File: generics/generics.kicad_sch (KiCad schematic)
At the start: 0 parts

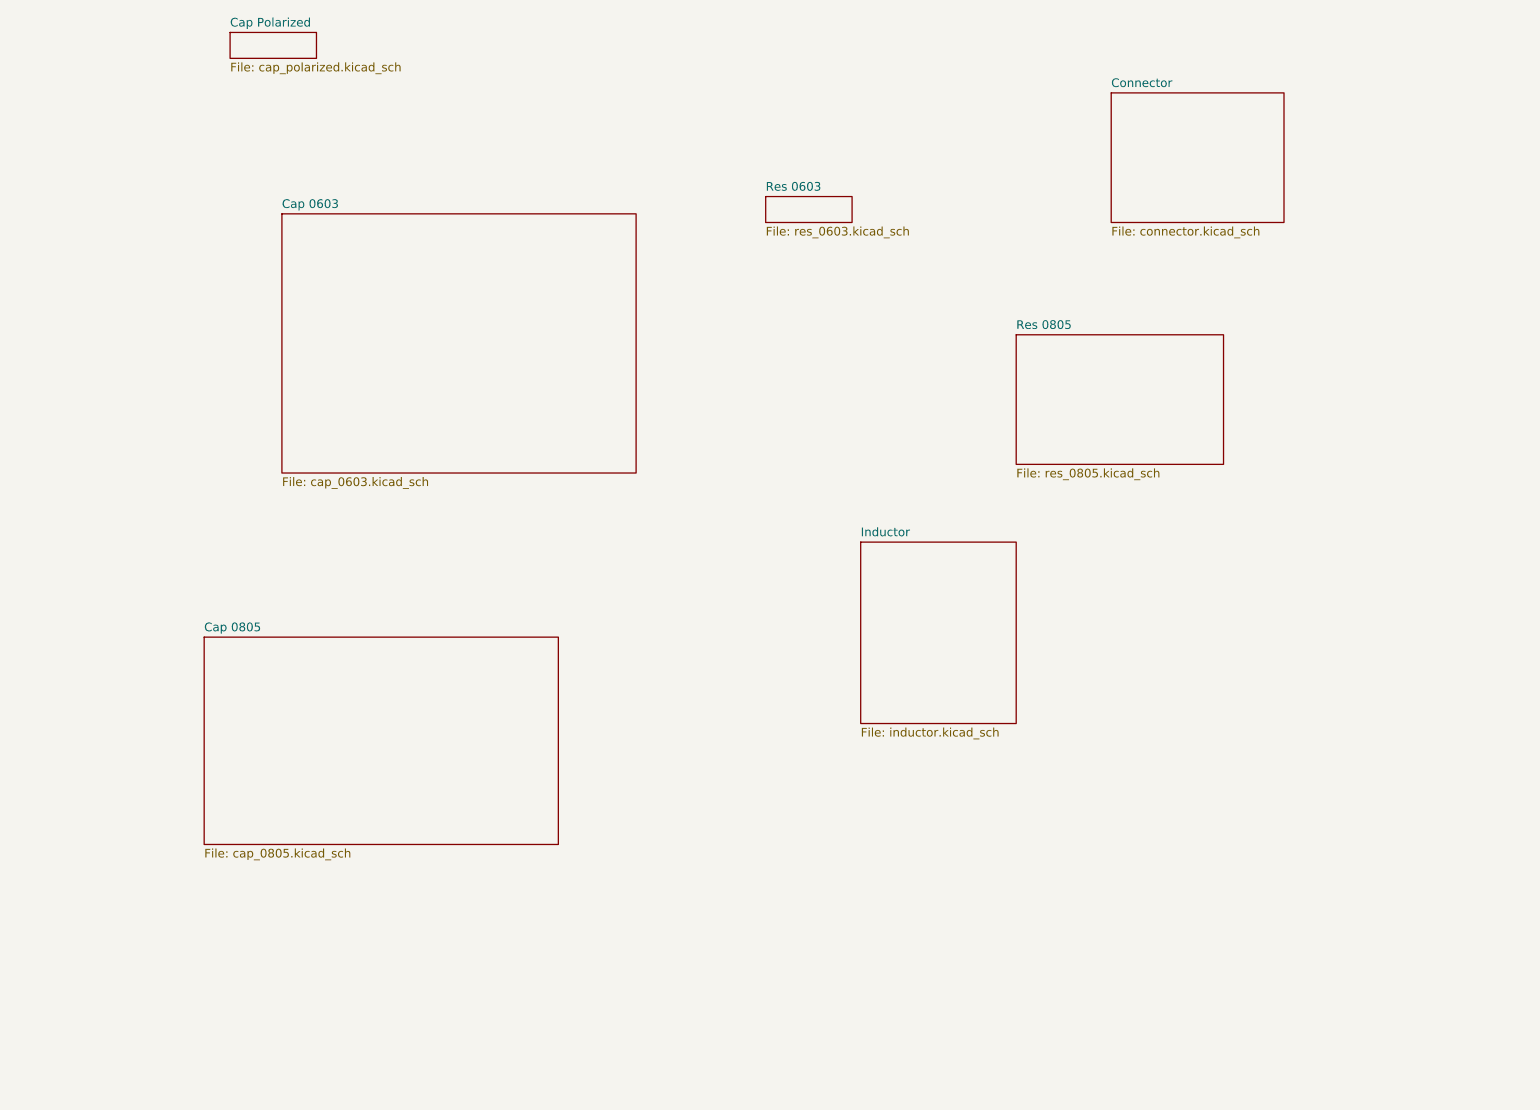
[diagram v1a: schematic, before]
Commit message: - Generics updates - Add LED library
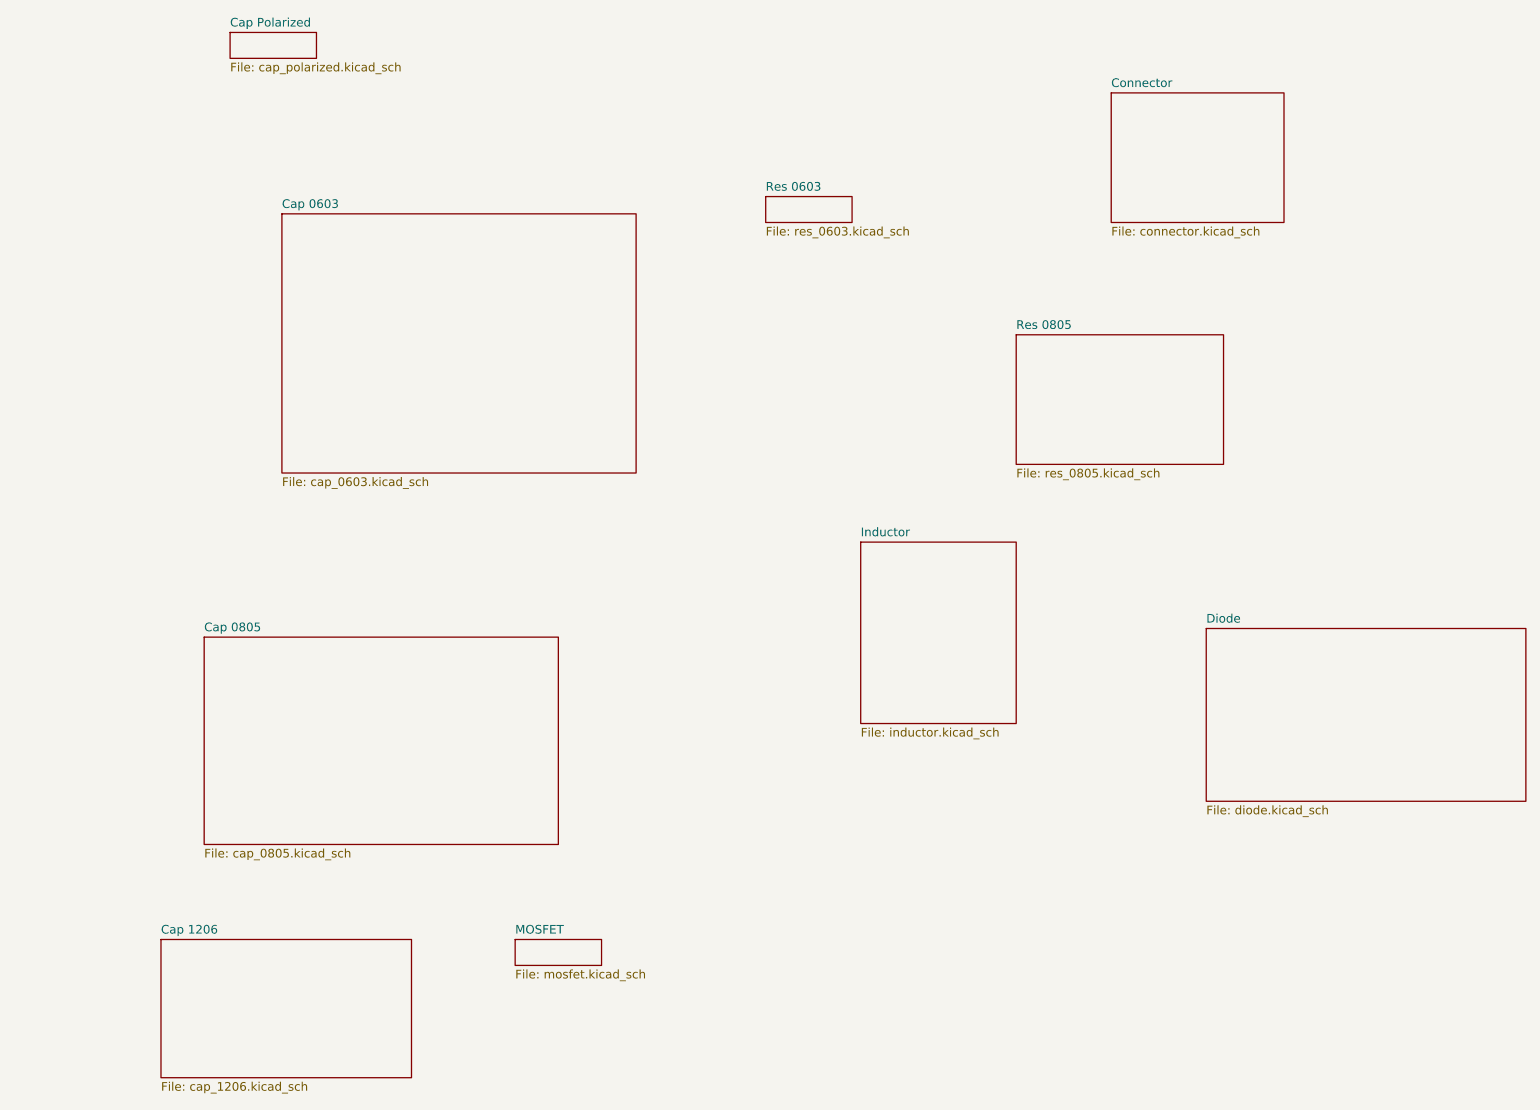
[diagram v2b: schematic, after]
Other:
- added sheet Cap 1206 (cap_1206.kicad_sch)
- added sheet Diode (diode.kicad_sch)
- added sheet MOSFET (mosfet.kicad_sch)
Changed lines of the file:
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@@
+	)
+	(sheet
+		(at 109.22 167.64)
+		(size 12.7 3.81)
+		(exclude_from_sim no)
+		(in_bom yes)
+		(on_board yes)
+		(dnp no)
+		(fields_autoplaced yes)
+		(stroke
+			(width 0.1524)
+			(type solid)
+		)
+		(fill
+			(color 0 0 0 0.0000)
+		)
+		(property "Sheetname" "MOSFET"
+			(at 109.22 166.9284 0)
+			(effects
+				(font
+					(size 1.27 1.27)
+				)
+				(justify left bottom)
+			)
+		)
+		(property "Sheetfile" "mosfet.kicad_sch"
+			(at 109.22 172.0346 0)
+			(effects
+				(font
+					(size 1.27 1.27)
+				)
+				(justify left top)
+			)
+		)
+		(instances
+			(project "generics"
+				(path "/ff075d90-2677-48ca-91fd-a3a441ca4e63"
+					(page "10")
+				)
+			)
+		)
 	)
 	(sheet
@@
 	)
 	(sheet
+		(at 210.82 121.92)
+		(size 46.99 25.4)
+		(exclude_from_sim no)
+		(in_bom yes)
+		(on_board yes)
+		(dnp no)
+		(fields_autoplaced yes)
+		(stroke
+			(width 0.1524)
+			(type solid)
+		)
+		(fill
+			(color 0 0 0 0.0000)
+		)
+		(property "Sheetname" "Diode"
+			(at 210.82 121.2084 0)
+			(effects
+				(font
+					(size 1.27 1.27)
+				)
+				(justify left bottom)
+			)
+		)
+		(property "Sheetfile" "diode.kicad_sch"
+			(at 210.82 147.9046 0)
+			(effects
+				(font
+					(size 1.27 1.27)
+				)
+				(justify left top)
+			)
+		)
+		(instances
+			(project "generics"
+				(path "/ff075d90-2677-48ca-91fd-a3a441ca4e63"
+					(page "9")
+				)
+			)
+		)
+	)
+	(sheet
 		(at 63.5 123.19)
 		(size 52.07 30.48)
@@
 				)
 			)
+		)
+	)
+	(sheet
+		(at 57.15 167.64)
+		(size 36.83 20.32)
+		(exclude_from_sim no)
+		(in_bom yes)
+		(on_board yes)
+		(dnp no)
+		(fields_autoplaced yes)
+		(stroke
+			(width 0.1524)
+			(type solid)
+		)
+		(fill
+			(color 0 0 0 0.0000)
+		)
+		(property "Sheetname" "Cap 1206"
+			(at 57.15 166.9284 0)
+			(effects
+				(font
+					(size 1.27 1.27)
+				)
+				(justify left bottom)
+			)
+		)
+		(property "Sheetfile" "cap_1206.kicad_sch"
+			(at 57.15 188.5446 0)
+			(effects
+				(font
+					(size 1.27 1.27)
+				)
+				(justify left top)
+			)
+		)
+		(instances
+			(project "generics"
+				(path "/ff075d90-2677-48ca-91fd-a3a441ca4e63"
+					(page "11")
+				)
+			)

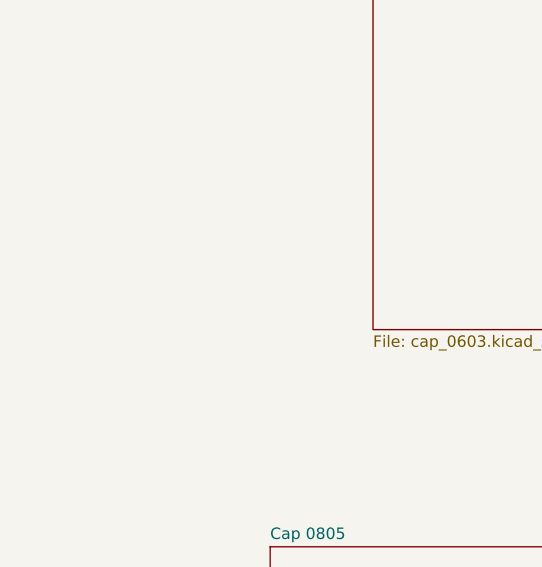
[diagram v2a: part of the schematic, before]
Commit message: Add parts for V0 status indicator light project
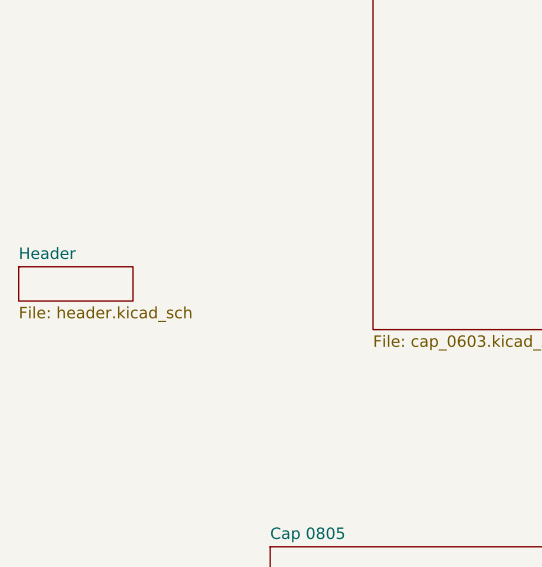
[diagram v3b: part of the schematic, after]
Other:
- added sheet Header (header.kicad_sch)
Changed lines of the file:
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@@
+	)
+	(sheet
+		(at 35.56 92.075)
+		(size 12.7 3.81)
+		(exclude_from_sim no)
+		(in_bom yes)
+		(on_board yes)
+		(dnp no)
+		(fields_autoplaced yes)
+		(stroke
+			(width 0.1524)
+			(type solid)
+		)
+		(fill
+			(color 0 0 0 0.0000)
+		)
+		(property "Sheetname" "Header"
+			(at 35.56 91.3634 0)
+			(effects
+				(font
+					(size 1.27 1.27)
+				)
+				(justify left bottom)
+			)
+		)
+		(property "Sheetfile" "header.kicad_sch"
+			(at 35.56 96.4696 0)
+			(effects
+				(font
+					(size 1.27 1.27)
+				)
+				(justify left top)
+			)
+		)
+		(instances
+			(project "generics"
+				(path "/ff075d90-2677-48ca-91fd-a3a441ca4e63"
+					(page "12")
+				)
+			)
+		)
 	)
 	(sheet
